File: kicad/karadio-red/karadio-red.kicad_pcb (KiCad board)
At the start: 2 copper layers, 48.3 x 40.6 mm, 18 parts, among them J1 CTRL, J2 PWR, J3 UART, J4 FW, J5 VS1053_RED, SW1 RESET, U1 AMS1117-3.3, U2 ESP-12E

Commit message: Improve KaRadio board
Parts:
- moved R5 0.13 mm to (207.0, 95.9)
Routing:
- net GNDD: track 196.5 -> 223.3 mm
- net Net-(R2-Pad2): track 28.1 -> 31.1 mm
- net /CS: track 29.7 -> 32.6 mm
- net /DREQ: track 35.8 -> 32.9 mm
- net /XCS: track 29.1 -> 26.3 mm
- net /MISO: track 25.7 -> 27.5 mm
- net /~RST: track 36.3 -> 37.3 mm
- net /ADC: track 41.8 -> 42.7 mm
- net /SCK: track 28.9 -> 29.8 mm
- net /XRESET: track 30.2 -> 30.9 mm
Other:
- board size 48.3 x 40.6 mm -> 48.3 x 41.3 mm
- rule via_min_size: 0.4 -> 0

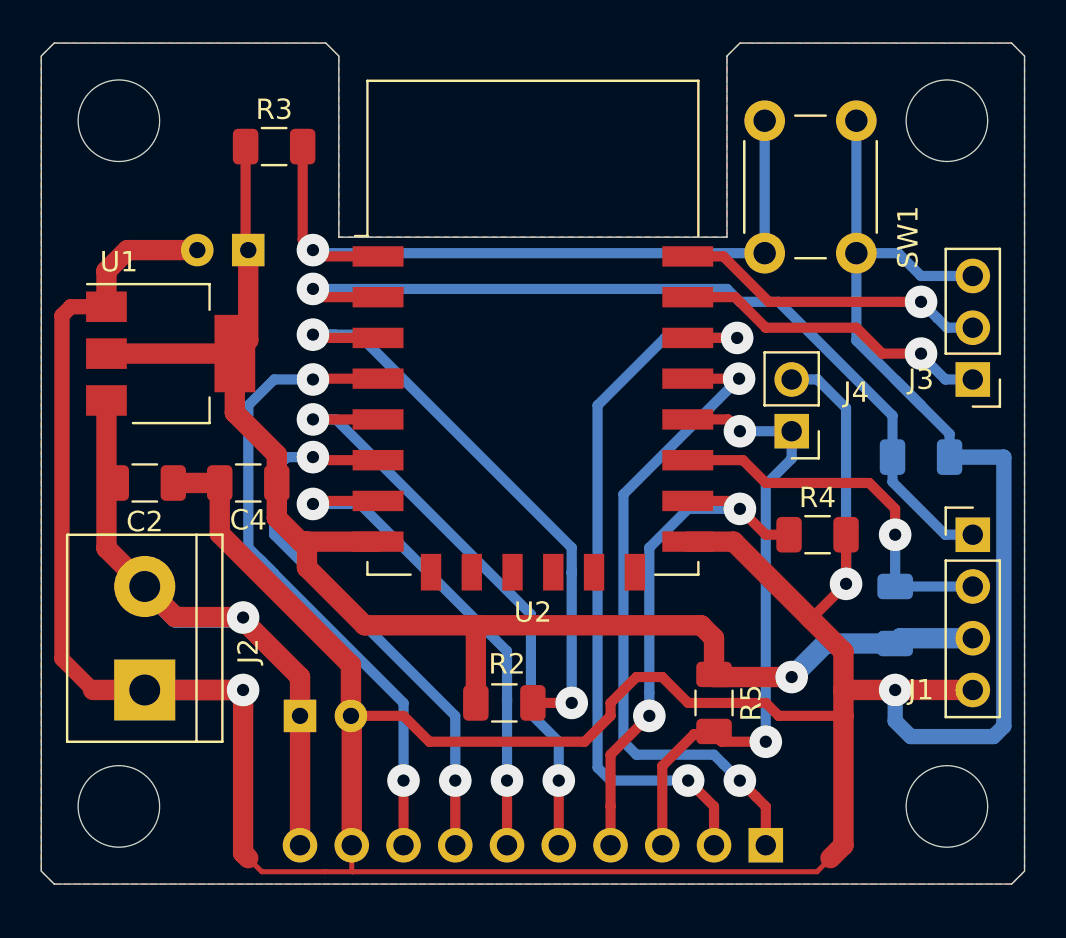
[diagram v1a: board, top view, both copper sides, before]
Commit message: Add optional RAM to karadio project
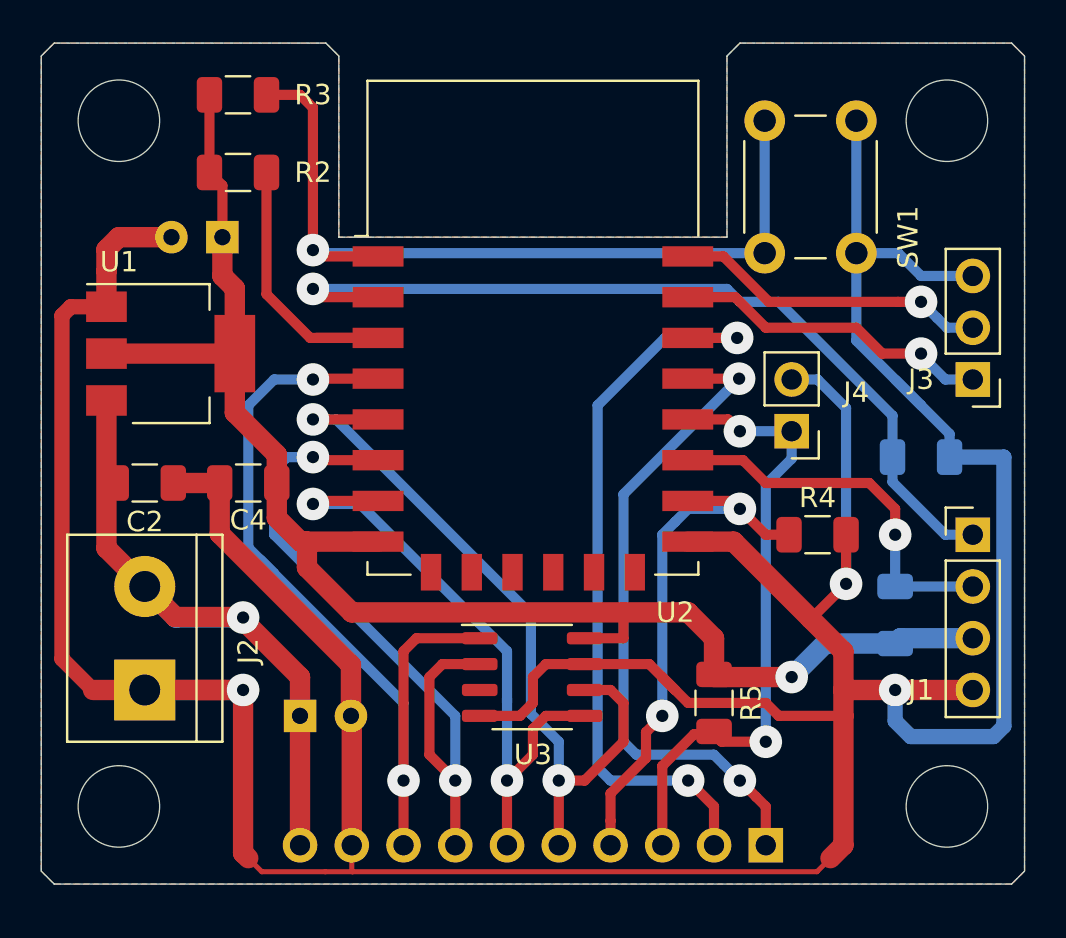
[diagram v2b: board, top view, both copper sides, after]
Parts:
- added U3: 23LCV1024, Package_SO:SO-8_3.9x4.9mm_P1.27mm, F.Cu at (198.1, 94.6)
- moved R2 29.1 mm to (183.6, 69.8)
- moved R3 3.10 mm to (183.6, 66.0)
- moved C3 1.42 mm to (182.9, 73.0)
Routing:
- net Net-(R2-Pad2): track 31.1 -> 15.4 mm, vias 2 -> 0
- net /CS: track 32.6 -> 43.0 mm
- net /MISO: track 27.5 -> 35.9 mm
- net /SCK: track 29.8 -> 37.8 mm
- net GNDD: track 223.3 -> 217.3 mm
- net /SI: track 25.5 -> 31.4 mm
- net /~RST: track 37.3 -> 41.6 mm
- net +3V3: track 73.2 -> 75.1 mm

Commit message: Make karadio project able to work with both 23LCV1024 and 23LC1024
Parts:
- added R7: 10k, Resistor_SMD:R_1206_3216Metric, F.Cu at (197.5, 91.4)
- added R8: 10k, Resistor_SMD:R_1206_3216Metric, F.Cu at (203.8, 91.4)
- added R9: 10k, Resistor_SMD:R_1206_3216Metric, F.Cu at (191.1, 91.4)
- moved J4 2.54 mm to (210.8, 80.0), turned to 0 degrees
- moved U2 1.91 mm to (198.1, 75.6)
- moved R5 1.42 mm to (208.3, 95.2)
- moved U3 1.40 mm to (197.5, 95.9)
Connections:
- U3 pad 7: GNDD -> Net-(R7-Pad2)
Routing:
- net Net-(R7-Pad2): track 0.00 -> 9.44 mm
- net Net-(R9-Pad2): track 0.00 -> 9.06 mm
- net /CS: track 43.0 -> 36.7 mm, vias 2 -> 3
- net +3V3: track 75.1 -> 81.5 mm
- net GNDD: track 217.3 -> 211.1 mm
- net /XRESET: track 30.9 -> 35.5 mm
- net Net-(R2-Pad2): track 15.4 -> 10.9 mm
- net /SCK: track 37.8 -> 42.3 mm
- net /SI: track 31.4 -> 35.3 mm
- net /MISO: track 35.9 -> 39.6 mm
- net /~RST: track 41.6 -> 38.6 mm
- net /XCS: track 26.3 -> 29.1 mm
- net /TX: track 15.4 -> 17.3 mm
- net /DREQ: track 32.9 -> 34.5 mm
- net /RX: track 15.6 -> 16.4 mm
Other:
- outline, holes or cut-outs redrawn

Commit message: Move karadio-red to Kicad 6
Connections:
- net /~RST renamed /~{RST}
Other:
- net class Default removed
